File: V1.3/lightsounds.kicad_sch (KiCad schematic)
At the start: 30 parts, among them J1 Conn_01x03_Male, J2 Conn_01x03_Female, SW1 SW_DIP_x04, T1 AO3400A, T2 AO3400A, T5 AO3400A, T6 AO3400A

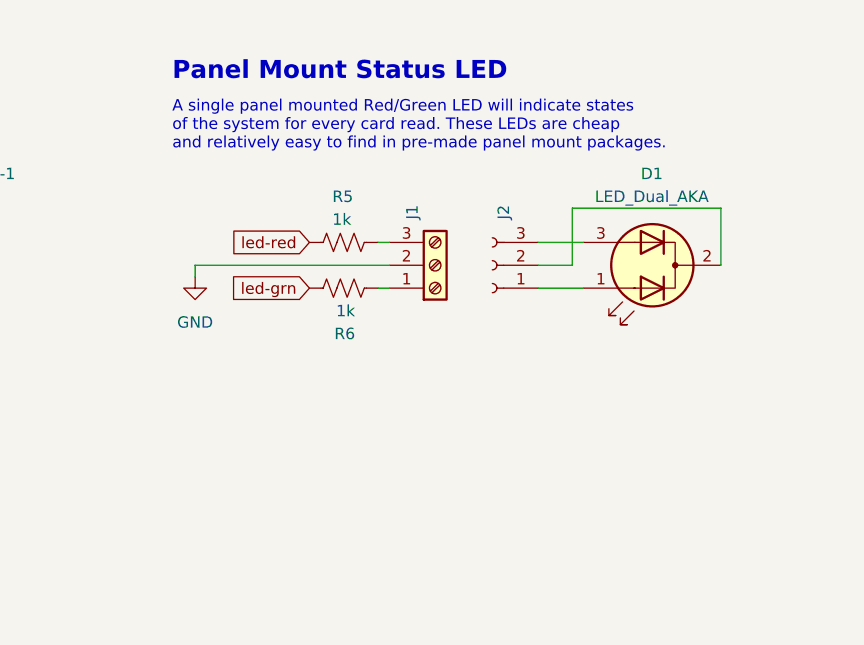
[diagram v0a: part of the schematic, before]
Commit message: fix(lightsounds): add bypass jumpers for the resistors on the indicator LEDS --> in case there is an indicator with resistors baked-in
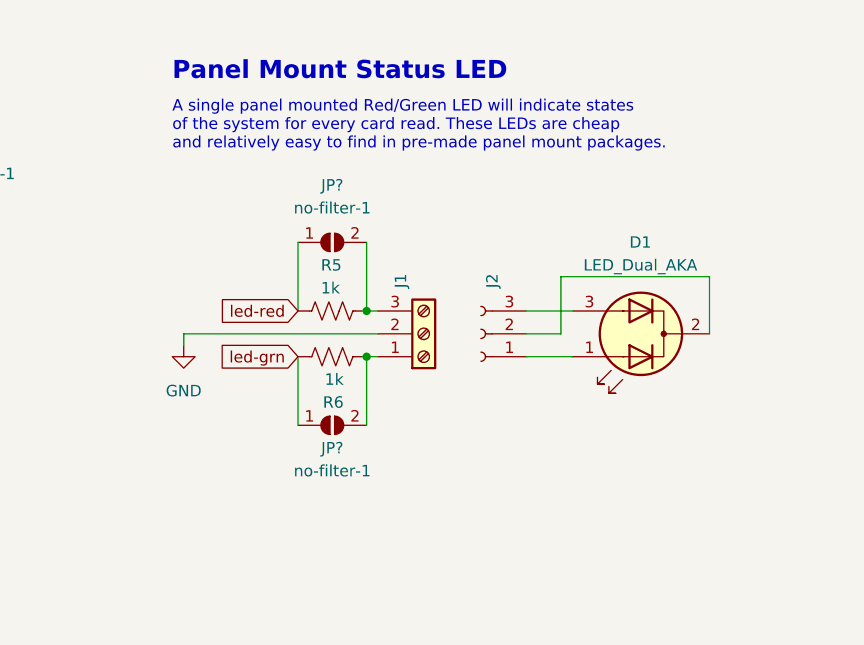
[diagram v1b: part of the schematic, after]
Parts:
- added JP? (x2): no-filter-1, Jumper:SolderJumper-2_P1.3mm_Open_RoundedPad1.0x1.5mm, symbol Jumper:SolderJumper_2_Open
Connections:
- net led-grn: now also JP?.1 (A)
- net led-red: now also JP?.1 (A)
- net at J1.3 (Pin_3), R5.2: now also JP?.2 (B)
- net at J1.1 (Pin_1), R6.1: now also JP?.2 (B)
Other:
- moved on the sheet: D1, J1, J2, R5, R6

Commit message: update v1.3 schematic documentation
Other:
- note added: "Lights, Sounds & Status"
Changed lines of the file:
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@@
     (effects (font (size 2 2) (thickness 0.4) bold) (justify left bottom))
+  )
+  (text "Lights, Sounds & Status" (at 39.37 35.56 0)
+    (effects (font (size 10 10) (thickness 2) bold italic) (justify left bottom))
   )
   (text "Using a few 'spare' pins, wee can read\nthe state of 4 dip switches to get \nfeedback in software about the board \nconfiguration (that we assume is correct)\n! see Docs for how to set switches !"

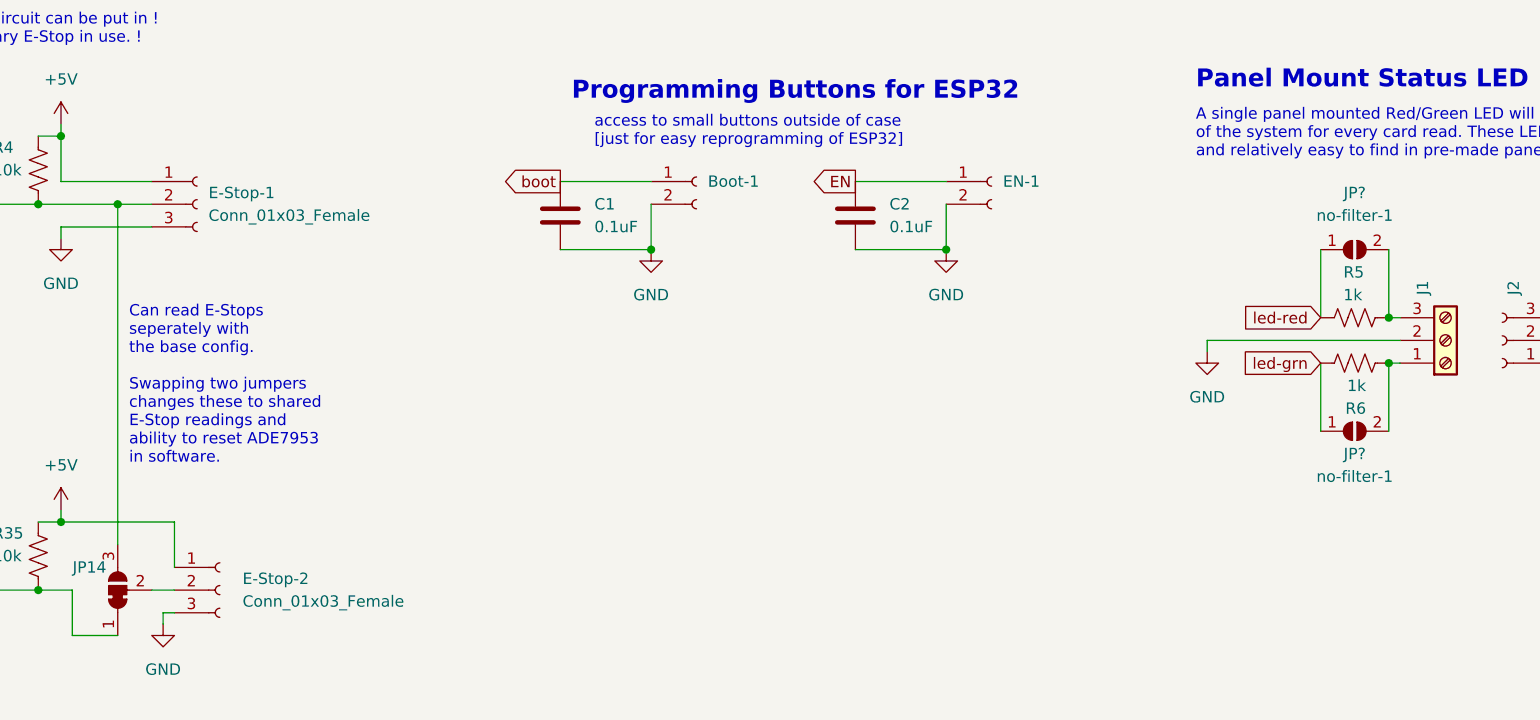
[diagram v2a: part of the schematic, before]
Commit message: fixes to board, based on Iris' feedback
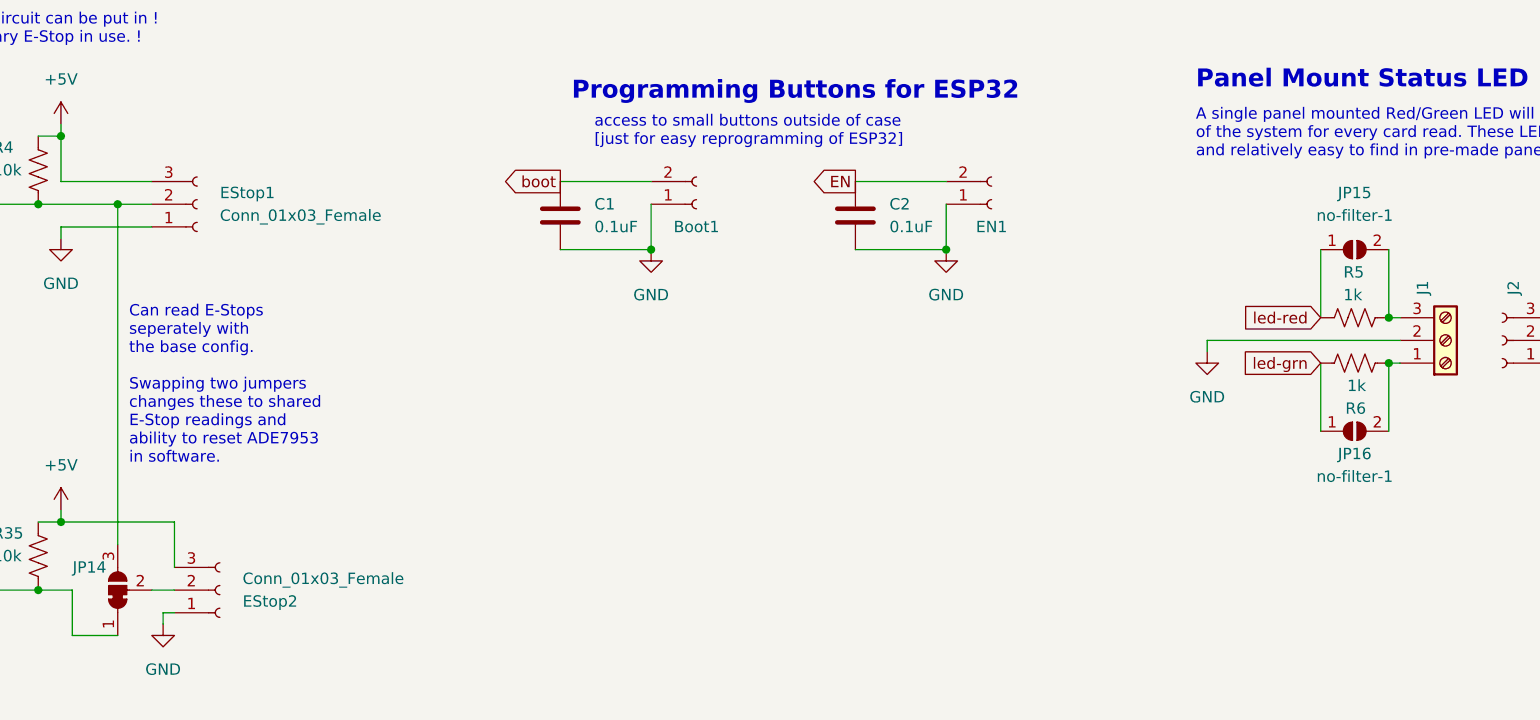
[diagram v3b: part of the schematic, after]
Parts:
- gave numbers to parts that had none: 2
- renumbered Boot-1 to Boot1, EN-1 to EN1, E-Stop-1 to EStop1, E-Stop-2 to EStop2
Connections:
- net +5V: now also EStop1.3 (Pin_3), EStop2.3 (Pin_3); no longer EStop1.1 (Pin_1), EStop2.1 (Pin_1)
- net EN: now also EN1.2 (Pin_2); no longer EN1.1 (Pin_1)
- net GND: now also Boot1.1 (Pin_1), EN1.1 (Pin_1), EStop1.1 (Pin_1), EStop2.1 (Pin_1); no longer Boot1.2 (Pin_2), EN1.2 (Pin_2), EStop1.3 (Pin_3), EStop2.3 (Pin_3)
- net boot: now also Boot1.2 (Pin_2); no longer Boot1.1 (Pin_1)

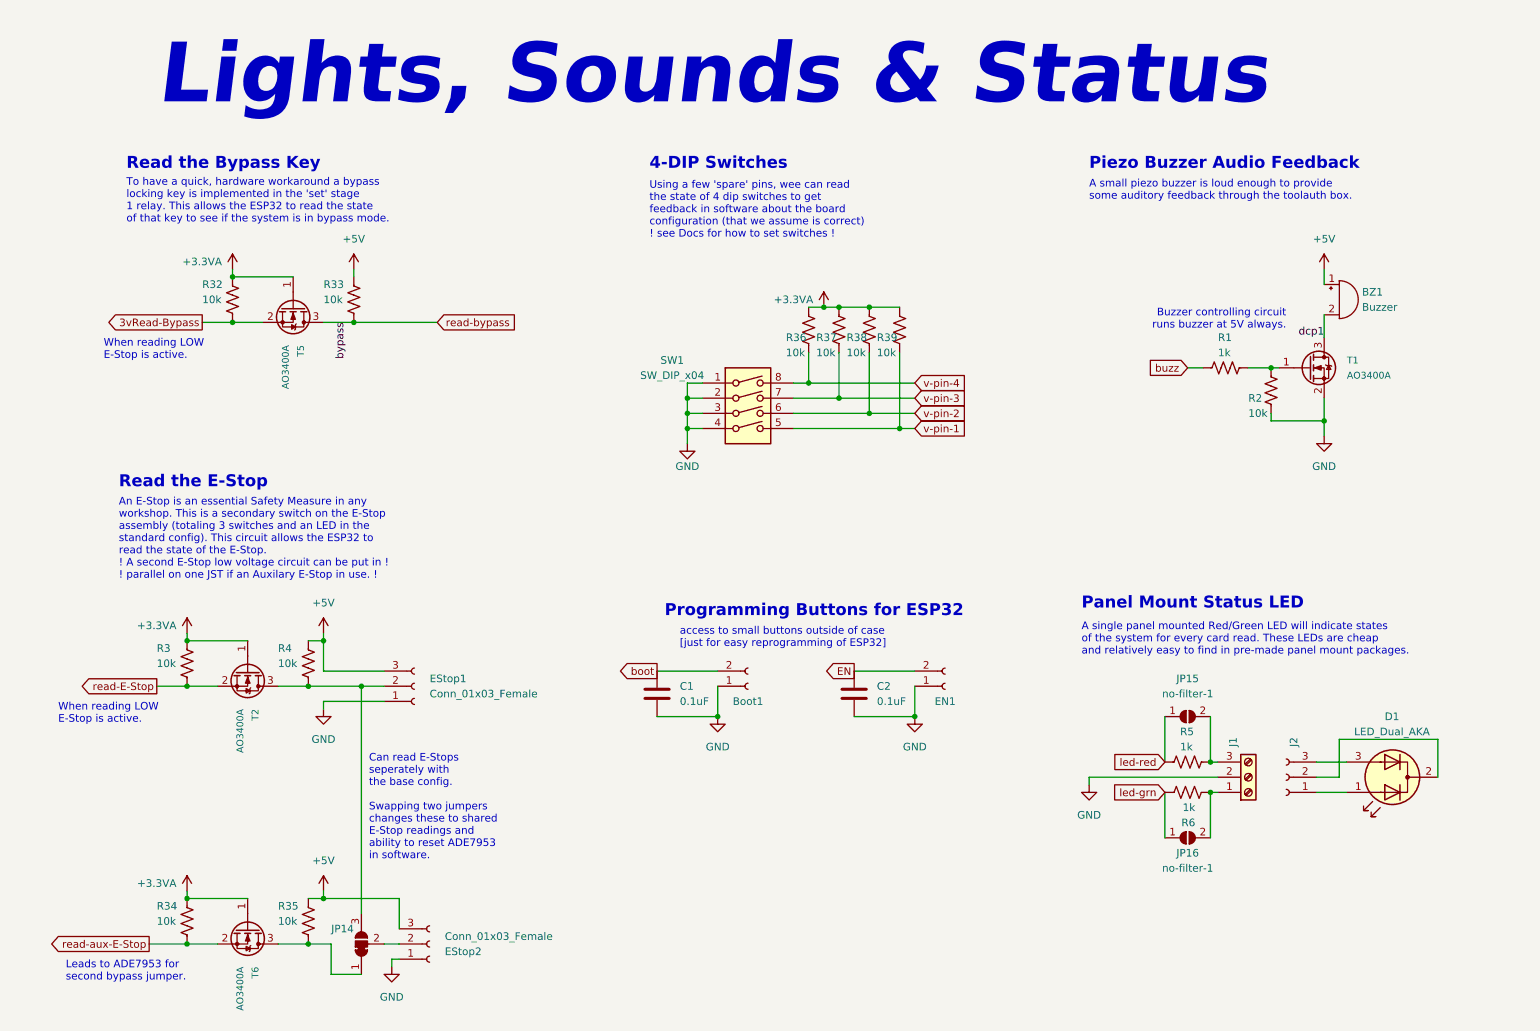
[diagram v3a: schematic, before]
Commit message: started adding the feather footprint to the board. need to update board shape and silkscreens
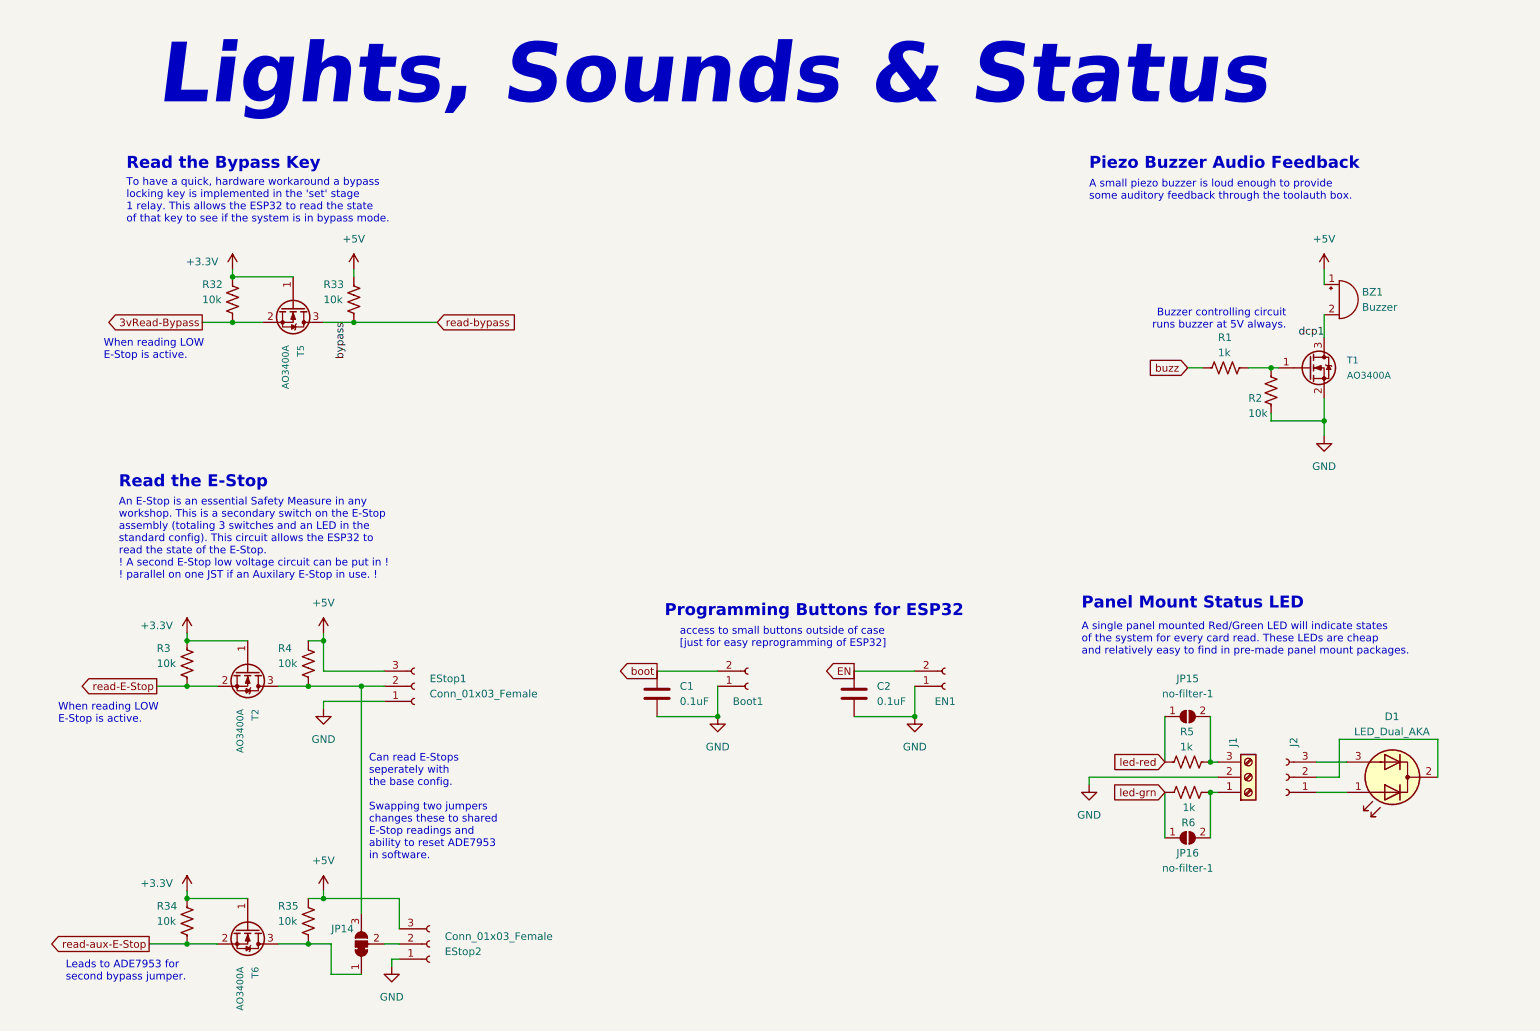
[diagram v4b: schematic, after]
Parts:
- removed R36, R37, R38, R39: 10k, Resistor_SMD:R_0603_1608Metric, symbol Device:R_US
- removed SW1: SW_DIP_x04, Button_Switch_SMD:SW_DIP_SPSTx04_Slide_Omron_A6H-4101_W6.15mm_P1.27mm, symbol Switch:SW_DIP_x04
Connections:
- net +3.3VA renamed +3.3V
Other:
- note removed: "4-DIP Switches"
- note removed: "Using a few 'spare' pins, wee can read the state of 4 dip switches to get feedback in software about the board configuration (that we assume is correct) ! see Docs for how to set switches !"

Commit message: design for feather-based board should work, but nothing is pretty
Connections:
- net +3.3V renamed +3.3VA
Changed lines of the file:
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@@
 			)
 		)
-		(property "Value" "+3.3V"
+		(property "Value" "+3.3VA"
 			(at 39.37 165.1 0)
 			(effects
@@
 			)
 		)
-		(property "Value" "+3.3V"
+		(property "Value" "+3.3VA"
 			(at 46.99 60.96 0)
 			(effects
@@
 			)
 		)
-		(property "Value" "+3.3V"
+		(property "Value" "+3.3VA"
 			(at 39.37 121.92 0)
 			(effects
